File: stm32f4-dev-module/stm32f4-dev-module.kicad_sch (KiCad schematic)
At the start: 42 parts, among them J1 SW, J2 Screw_Terminal_CAN, J3 I2C1, J4 SPI1, P1 USB_C_Plug, SW1 SW_SPST, SW2 SW_SPDT, SW3 SW_DPST, U1 STM32F405RGT6, U2 USBLC6-2SC6, U3 SN65HVD230, U4 AP2112K-3.3, U5 ICM-42670-P, Y1 25MHz

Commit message: Release V1.0
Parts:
- removed C12: 4u7, symbol Device:C_Polarized_Small
- removed J2: Screw_Terminal_CAN, symbol Connector:Screw_Terminal_01x02
- removed P1: USB_C_Plug, symbol Connector:USB_C_Plug
- removed SW2: SW_SPDT, symbol Switch:SW_SPDT
- removed SW3: SW_DPST, symbol Switch:SW_DPST
- removed U5: ICM-42670-P, symbol eggsacc:ICM-42670-P
- added C22, C23, C24: 100n, Capacitor_SMD:C_0402_1005Metric, symbol Device:C_Small
- added J10: Screw_Terminal_01x03, TerminalBlock_Phoenix:TerminalBlock_Phoenix_MKDS-1-3-3.81_1x03_P3.81mm_Horizontal, symbol Connector:Screw_Terminal_01x03
- added J11: Conn_02x10_Odd_Even, Connector_PinHeader_2.54mm:PinHeader_2x10_P2.54mm_Vertical, symbol Connector_Generic:Conn_02x10_Odd_Even
- added J5: 5V_IN, Connector_PinHeader_2.54mm:PinHeader_1x02_P2.54mm_Vertical, symbol Connector:Conn_01x02_Socket
- added J6: OLED, addons:OLED header, symbol Connector:Conn_01x04_Pin
- added J7: USB_C_Receptacle_USB2.0_16P, Connector_USB:USB_C_Receptacle_G-Switch_GT-USB-7010ASV, symbol Connector:USB_C_Receptacle_USB2.0_16P
- added J8: USART3, Connector_PinHeader_2.54mm:PinHeader_1x04_P2.54mm_Vertical, symbol Connector:Conn_01x04_Pin
- added J9: PWM, Connector_PinHeader_2.54mm:PinHeader_2x03_P2.54mm_Vertical, symbol Connector_Generic:Conn_02x03_Top_Bottom
- added R10, R12: 10k, Resistor_SMD:R_0402_1005Metric, symbol Device:R_Small
- added R11, R9: 100, Resistor_SMD:R_0402_1005Metric, symbol Device:R_Small
- added R6: 0, Resistor_SMD:R_0603_1608Metric, symbol Device:R_Small
- added R7, R8: 5k1, Resistor_SMD:R_0402_1005Metric, symbol Device:R_Small
- added SW5, SW6: BTN_UTIL, addons:SW-SMD_4P-L4.2-W3.4-P2.15-LS5.2, symbol symlib:HX 3X4X2.5-PA-4N PUSH BUTTON SWITCH
- added SW7: BTN_NRST, addons:SW-SMD_4P-L4.2-W3.4-P2.15-LS5.2, symbol symlib:HX 3X4X2.5-PA-4N PUSH BUTTON SWITCH
- C1, C10, C11, C13, C16, C17, C2, C21, C3, C4, C5, C7, C8, C9: footprint (none) -> Capacitor_SMD:C_0402_1005Metric
- C14, C15, C19, C6: footprint (none) -> Capacitor_SMD:C_0603_1608Metric
- C18: value 100n -> 2u2; footprint (none) -> Capacitor_SMD:C_0603_1608Metric
- C20: value 10n -> 4u7; footprint (none) -> Capacitor_SMD:C_0603_1608Metric
- D1: value RED -> GREEN; footprint (none) -> LED_SMD:LED_0402_1005Metric
- FB1: footprint (none) -> Inductor_SMD:L_0603_1608Metric
- J1: value SW -> SWD; footprint (none) -> Connector_JST:JST_SH_SM04B-SRSS-TB_1x04-1MP_P1.00mm_Horizontal
- J3: footprint (none) -> Connector_PinHeader_2.54mm:PinHeader_1x04_P2.54mm_Vertical
- J4: footprint Connector_PinHeader_1.00mm:PinHeader_2x03_P1.00mm_Vertical -> Connector_PinHeader_2.54mm:PinHeader_2x03_P2.54mm_Vertical
- R1, R3, R4, R5: footprint (none) -> Resistor_SMD:R_0402_1005Metric
- R2: value 1k -> 330; footprint (none) -> Resistor_SMD:R_0402_1005Metric
- SW1: value SW_SPST -> BOOT0; footprint (none) -> Button_Switch_SMD:SW_DIP_SPSTx01_Slide_6.7x4.1mm_W6.73mm_P2.54mm_LowProfile_JPin
- U4: footprint Connector_USB:USB_C_Plug_Molex_105444 -> Package_TO_SOT_SMD:SOT-23-5_HandSoldering
- Y1: footprint (none) -> Crystal:Crystal_SMD_3225-4Pin_3.2x2.5mm
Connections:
- net +3.3V: now also J1.3 (Pin_3), J3.2 (Pin_2), J4.1 (Pin_1), SW1.1 (A), J11.1 (Pin_1), J11.2 (Pin_2), J8.2 (Pin_2), R10.2, R12.2; no longer C18.1, C19.1, C20.1, J1.4 (Pin_4), J3.4 (Pin_4), J4.4 (Pin_4)
- net BOOT0: now also SW1.2 (B)
- net CANH: now also J10.3 (Pin_3)
- net CANL: now also J10.2 (Pin_2)
- net GND: now also J1.4 (Pin_4), J4.3 (Pin_3), R1.1, C22.2, C23.2, C24.2, J10.1 (Pin_1), J11.5 (Pin_5), J11.6 (Pin_6), J5.2 (Pin_2), J6.1 (Pin_1), J7.A1 (GND), J7.A12 (GND), J7.B1 (GND), J7.B12 (GND), J7.SH (SHIELD), J8.1 (Pin_1), R7.1, R8.1, SW5.1, SW5.3, SW6.1, SW6.3, SW7.1, SW7.3; no longer J1.1 (Pin_1), J4.6 (Pin_6), SW1.1 (A)
- net I2C1_SCL: now also J3.3 (Pin_3); no longer J3.2 (Pin_2)
- net I2C1_SDA: now also J3.4 (Pin_4); no longer J3.3 (Pin_3)
- net NRST: now also SW7.2, SW7.4; no longer SW1.2 (B)
- net SPI1_CLK: now also J4.5 (Pin_5); no longer J4.2 (Pin_2)
- net SPI1_CS: now also J4.6 (Pin_6); no longer J4.3 (Pin_3)
- net SPI1_MISO: now also J4.4 (Pin_4); no longer J4.1 (Pin_1)
- net SPI1_MOSI: now also J4.2 (Pin_2); no longer J4.5 (Pin_5)
- net SWDIO: now also J1.1 (Pin_1); no longer J1.3 (Pin_3)
- net D+: now reaches U2.3 (I/O2)
- net D+: now also J7.A6 (D+), J7.B6 (D+)
- net D-: now reaches U2.1 (I/O1)
- net D-: now also J7.A7 (D-), J7.B7 (D-)
- net at R5.1: now also R4.1, R6.2
- net at C21.1: now also R6.1
- net PC2: now reaches U1.10 (PC2)
- net PC2: now also J11.10 (Pin_10)
- net PC3: now reaches U1.11 (PC3)
- net PC3: now also J11.11 (Pin_11)
- net PA0: now reaches U1.14 (PA0)
- net PA0: now also J11.12 (Pin_12)
- net PA1: now reaches U1.15 (PA1)
- net PA1: now also J11.13 (Pin_13)
- net TIM1_CH2N: now reaches U1.26 (PB0)
- net TIM1_CH2N: now also J9.4 (Pin_4)
- net TIM1_CH3N: now reaches U1.27 (PB1)
- net TIM1_CH3N: now also J9.2 (Pin_2)
- net I2C2_SCL: now reaches U1.29 (PB10)
- net I2C2_SCL: now also J6.3 (Pin_3)
- net I2C2_SDA: now reaches U1.30 (PB11)
- net I2C2_SDA: now also J6.4 (Pin_4)
- net VCAP_1: now reaches U1.31 (VCAP_1)
- net VCAP_1: now also C19.1
- net PB12: now reaches U1.33 (PB12)
- net PB12: now also J11.20 (Pin_20)
- net TIM1_CH1N: now reaches U1.34 (PB13)
- net TIM1_CH1N: now also J9.6 (Pin_6)
- net PB14: now reaches U1.35 (PB14)
- net PB14: now also J11.19 (Pin_19)
- net PB15: now reaches U1.36 (PB15)
- net PB15: now also J11.18 (Pin_18)
- net PC6: now reaches U1.37 (PC6)
- net PC6: now also J11.17 (Pin_17)
- net PC7: now reaches U1.38 (PC7)
- net PC7: now also J11.16 (Pin_16)
- net PC8: now reaches U1.39 (PC8)
- net PC8: now also J11.15 (Pin_15)
- net PC9: now reaches U1.40 (PC9)
- net PC9: now also J11.14 (Pin_14)
- net TIM1_CH1: now reaches U1.41 (PA8)
- net TIM1_CH1: now also J9.5 (Pin_5)
- net TIM1_CH2: now reaches U1.42 (PA9)
- net TIM1_CH2: now also J9.3 (Pin_3)
- net TIM1_CH3: now reaches U1.43 (PA10)
- net TIM1_CH3: now also J9.1 (Pin_1)
- net VCAP_2: now reaches U1.47 (VCAP_2)
- net VCAP_2: now also C18.1
- net USART3_TX: now reaches U1.51 (PC10)
- net USART3_TX: now also J8.3 (Pin_3)
- net USART3_RX: now reaches U1.52 (PC11)
- net USART3_RX: now also J8.4 (Pin_4)
- net PC12: now reaches U1.53 (PC12)
- net PC12: now also J11.9 (Pin_9)
- net PB3: now reaches U1.55 (PB3)
- net PB3: now also J11.8 (Pin_8)
- net PB4: now reaches U1.56 (PB4)
- net PB4: now also J11.7 (Pin_7)
- net ACCEL_CS: no longer names the net of U1.17 (PA3)
- net ACCEL_CS: now also C23.1, R11.2, R12.1
- net ACCEL_INT: no longer names the net of U1.16 (PA2)
- net ACCEL_INT: now also C22.1, R10.1, R9.2
- net VBUS renamed +5V
- net +5V: now also C20.1, C24.1, J11.3 (Pin_3), J11.4 (Pin_4), J5.1 (Pin_1), J6.2 (Pin_2), J7.A4 (VBUS), J7.A9 (VBUS), J7.B4 (VBUS), J7.B9 (VBUS)
- new net: J7.A5 (CC1), R8.2
- new net: R9.1, SW5.2, SW5.4
- new net: J7.B5 (CC2), R7.2
- new net: R11.1, SW6.2, SW6.4
- no-connect marks 17 -> 14
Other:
- note added: "0R bus termination select"
- note added: "12pF crystal C =2*(C_crys - C_stray) =2*(12-5) =14pF"
- note added: "CAN"
- note added: "Comm headers"
- note added: "LDO"
- note added: "MCU"
- note added: "OSC"
- note added: "Pin breakout"
- note added: "USB"
- note added: "Utility buttons"
- moved on the sheet: C10, C11, C13, C14, C15, C21, D1, J1, J3, J4, R2, U2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

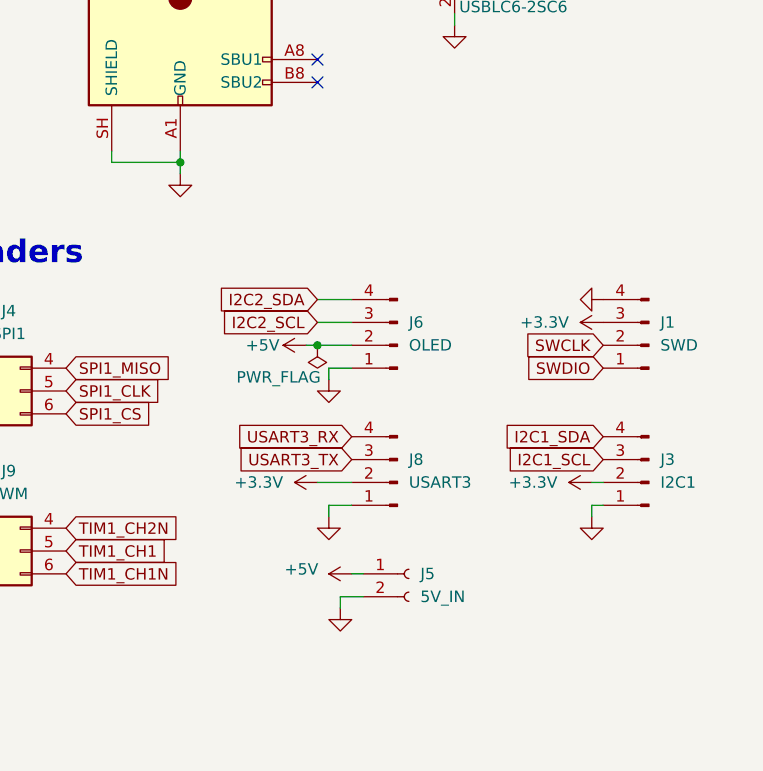
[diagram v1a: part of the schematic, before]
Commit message: Dev. module V1.1: added pull up resistors to i2c lines.
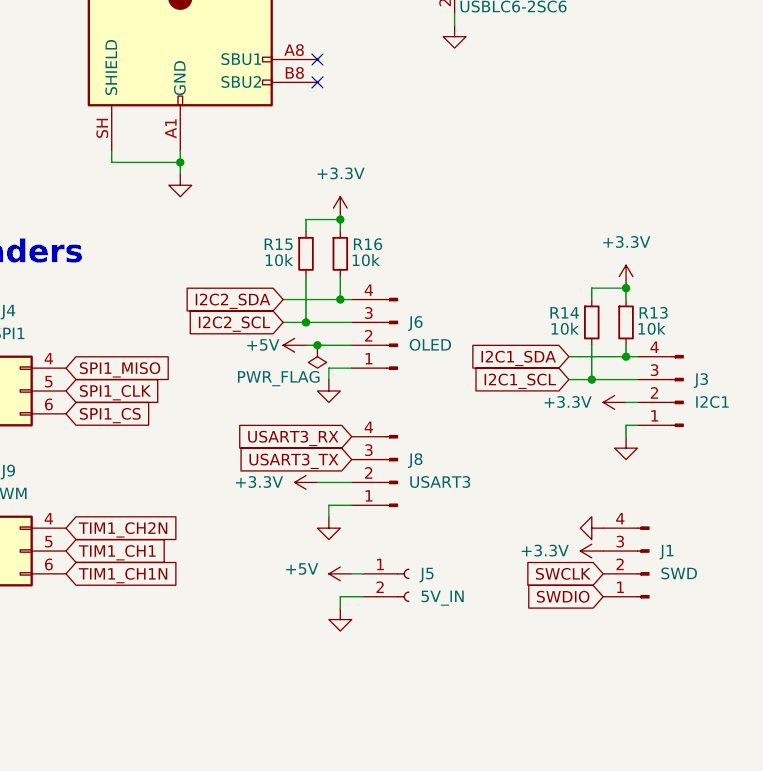
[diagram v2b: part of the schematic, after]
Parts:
- added R13, R14, R15, R16: 10k, Resistor_SMD:R_0402_1005Metric, symbol Device:R_Small
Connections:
- net +3.3V: now also R13.1, R14.1, R15.1, R16.1
- net I2C1_SCL: now also R14.2
- net I2C1_SDA: now also R13.2
- net I2C2_SCL: now also R15.2
- net I2C2_SDA: now also R16.2
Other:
- moved on the sheet: J1, J3
